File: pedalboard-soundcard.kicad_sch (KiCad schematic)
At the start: 5 parts, among them J1 RPi_GPIO

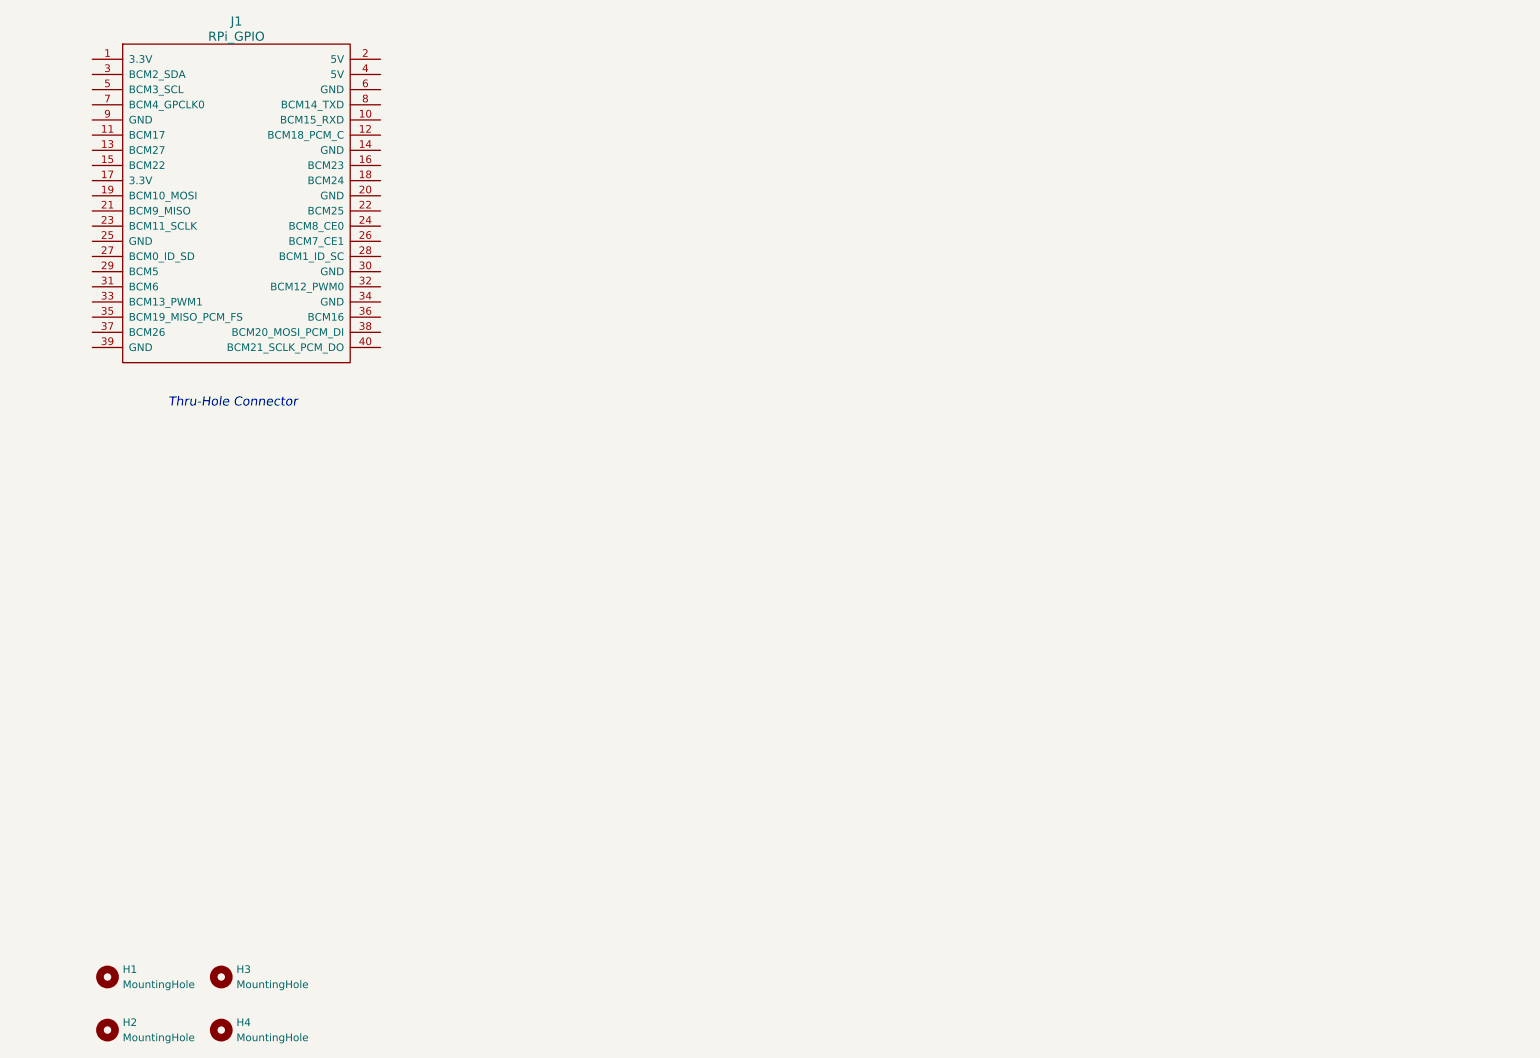
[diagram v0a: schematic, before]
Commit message: First placement of parts on PCB
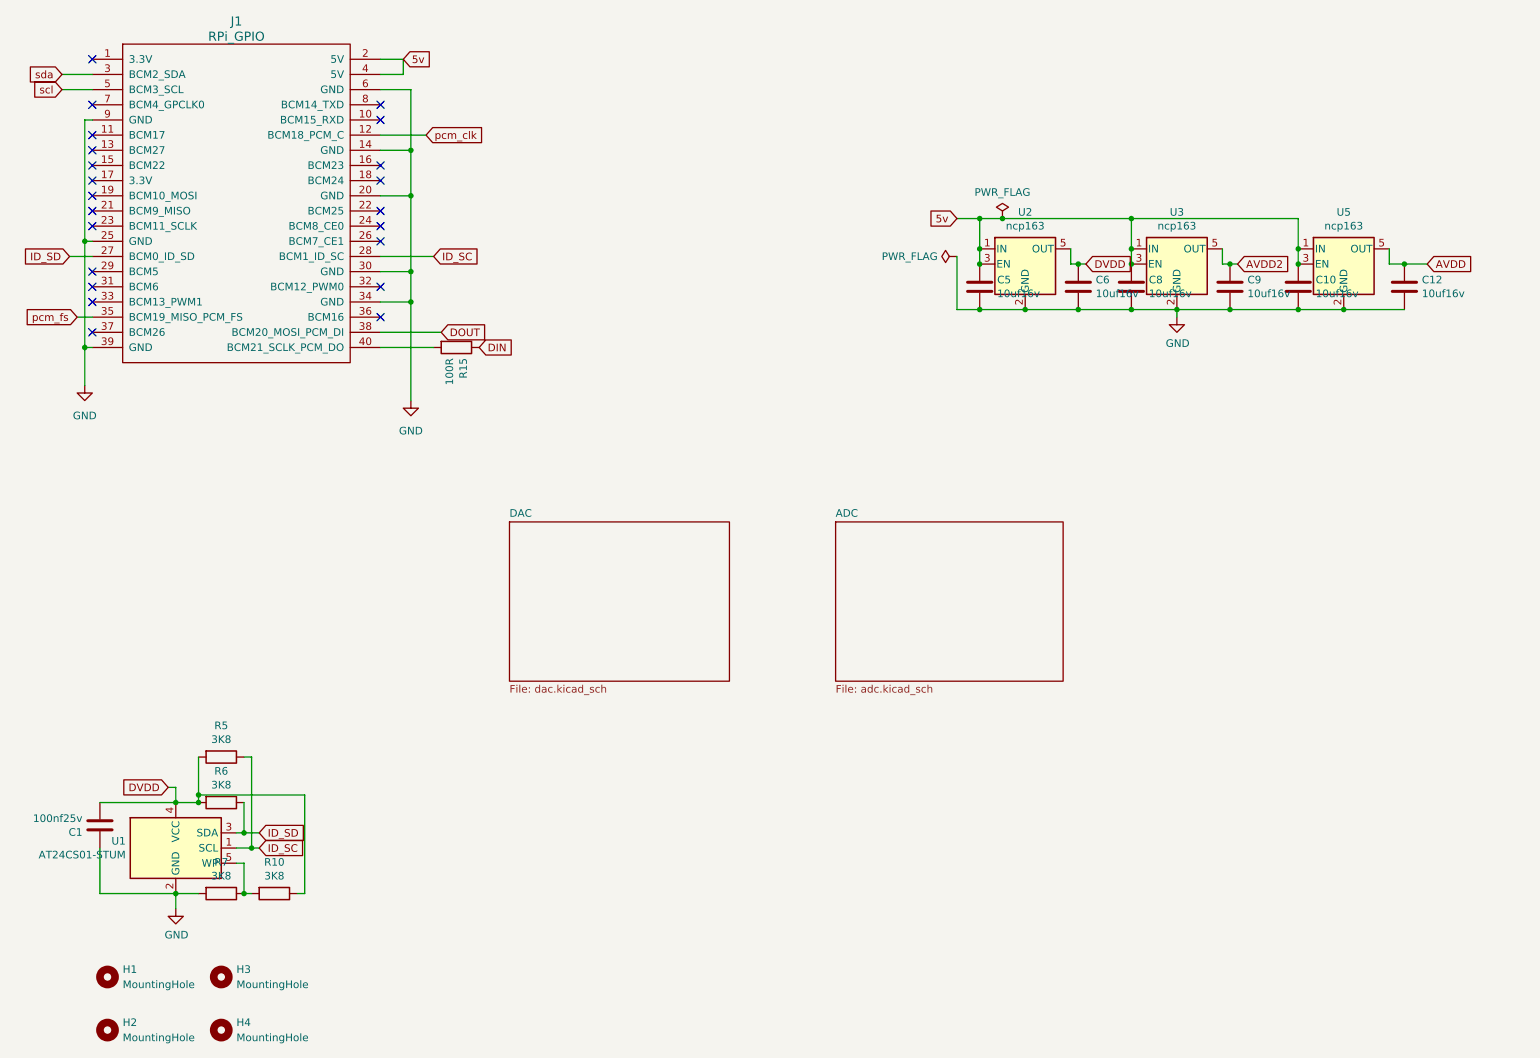
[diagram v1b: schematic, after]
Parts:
- added C1: 100nf25v, Capacitor_SMD:C_0805_2012Metric, symbol Device:C
- added C10, C12, C5, C6, C8, C9: 10uf16v, Capacitor_SMD:C_0805_2012Metric, symbol Device:C
- added R10, R5, R6, R7: 3K8, Resistor_SMD:R_0805_2012Metric, symbol Device:R
- added R15: 100R, Resistor_SMD:R_0805_2012Metric, symbol Device:R
- added U1: AT24CS01-STUM, Package_TO_SOT_SMD:SOT-23-5, symbol Memory_EEPROM:AT24CS01-STUM
- added U2, U3, U5: ncp163, Package_TO_SOT_SMD:SOT-23-5, symbol zynthiandac-rescue:TLV71333PDBV-Regulator_Linear
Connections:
- net pcm_clk: now reaches J1.12 (BCM18_PCM_C)
- net GND: now reaches J1.14 (GND)
- net GND: now also J1.20 (GND), J1.25 (GND), J1.30 (GND), J1.34 (GND), J1.39 (GND), J1.6 (GND), J1.9 (GND), C1.1, C10.2, C12.2, C5.2, C6.2, C8.2, C9.2, R7.2, U1.2 (GND), U2.2 (GND), U3.2 (GND), U5.2 (GND)
- net 5v: now reaches J1.2 (5V)
- net 5v: now also J1.4 (5V), C10.1, C5.1, C8.1, U2.1 (IN), U2.3 (EN), U3.1 (IN), U3.3 (EN), U5.1 (IN), U5.3 (EN)
- net ID_SD: now reaches J1.27 (BCM0_ID_SD)
- net ID_SD: now also R6.1, U1.3 (SDA)
- net ID_SC: now reaches J1.28 (BCM1_ID_SC)
- net ID_SC: now also R5.1, U1.1 (SCL)
- net sda: now reaches J1.3 (BCM2_SDA)
- net pcm_fs: now reaches J1.35 (BCM19_MISO_PCM_FS)
- net DOUT: now reaches J1.38 (BCM20_MOSI_PCM_DI)
- net at J1.40 (BCM21_SCLK_PCM_DO): now also R15.2
- net scl: now reaches J1.5 (BCM3_SCL)
- new net: R10.2, R7.1, U1.5 (WP)
- new net AVDD: C12.1, U5.5 (OUT)
- new net AVDD2: C9.1, U3.5 (OUT)
- new net DIN: R15.1
- new net DVDD: C1.2, C6.1, R10.1, R5.2, R6.2, U1.4 (VCC), U2.5 (OUT)
- no-connect marks 0 -> 22
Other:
- added sheet ADC (adc.kicad_sch)
- added sheet DAC (dac.kicad_sch)
- note removed: "Thru-Hole Connector"

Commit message: Page settings
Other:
- company: (none) -> github.com/pedalboard
- title: (none) -> Open Pedalboard Soundcard
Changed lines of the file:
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@@
 (kicad_sch (version 20230121) (generator eeschema)
   (paper "A4")
+  (title_block
+    (title "Open Pedalboard Soundcard")
+    (date "2023-12-19")
+    (rev "0.0.1")
+    (company "github.com/pedalboard")
+    (comment 1 "Source Code: https://github.com/pedalboard/pedalboard-hw")
+    (comment 2 "License: CERN Open Hardware Licence Version 2 - Permissive")
+  )
   (junction (at 172.72 68.58) (diameter 0) (color 0 0 0 0)
   )

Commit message: Distribute parts on PCB
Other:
- moved on the sheet: C1, R10, R5, R6, R7, U1

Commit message: Cleanup placement
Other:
- moved on the sheet: C10, C12, C5, C6, C8, C9, U2, U3, U5

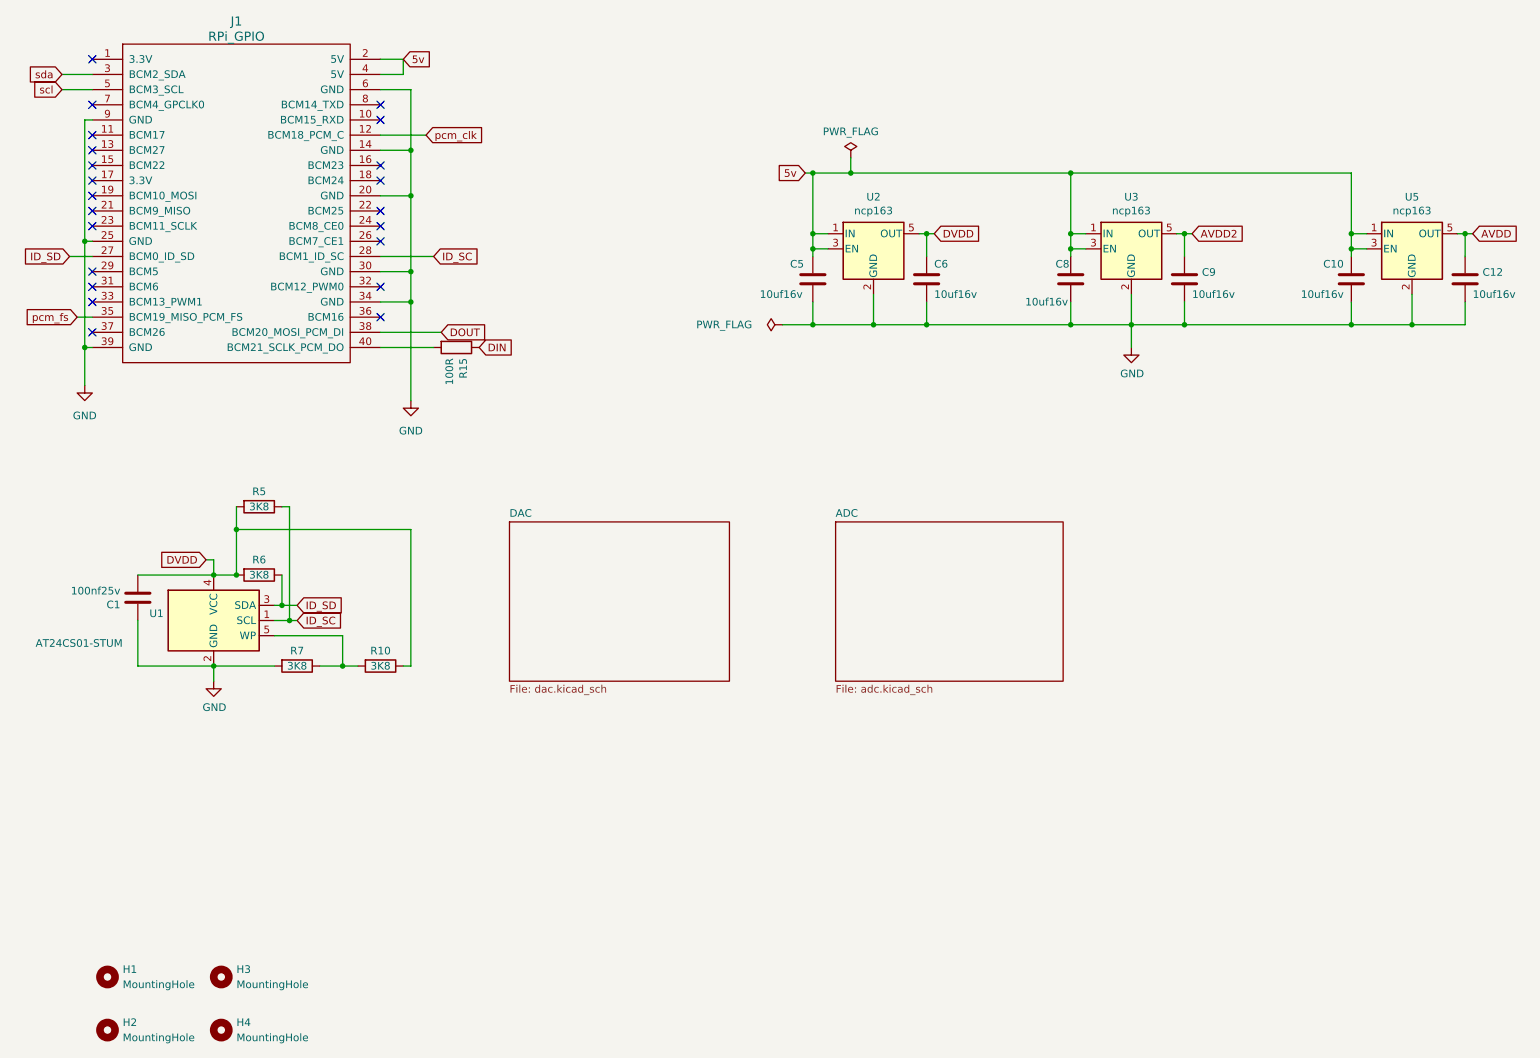
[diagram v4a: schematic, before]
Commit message: improve BOM
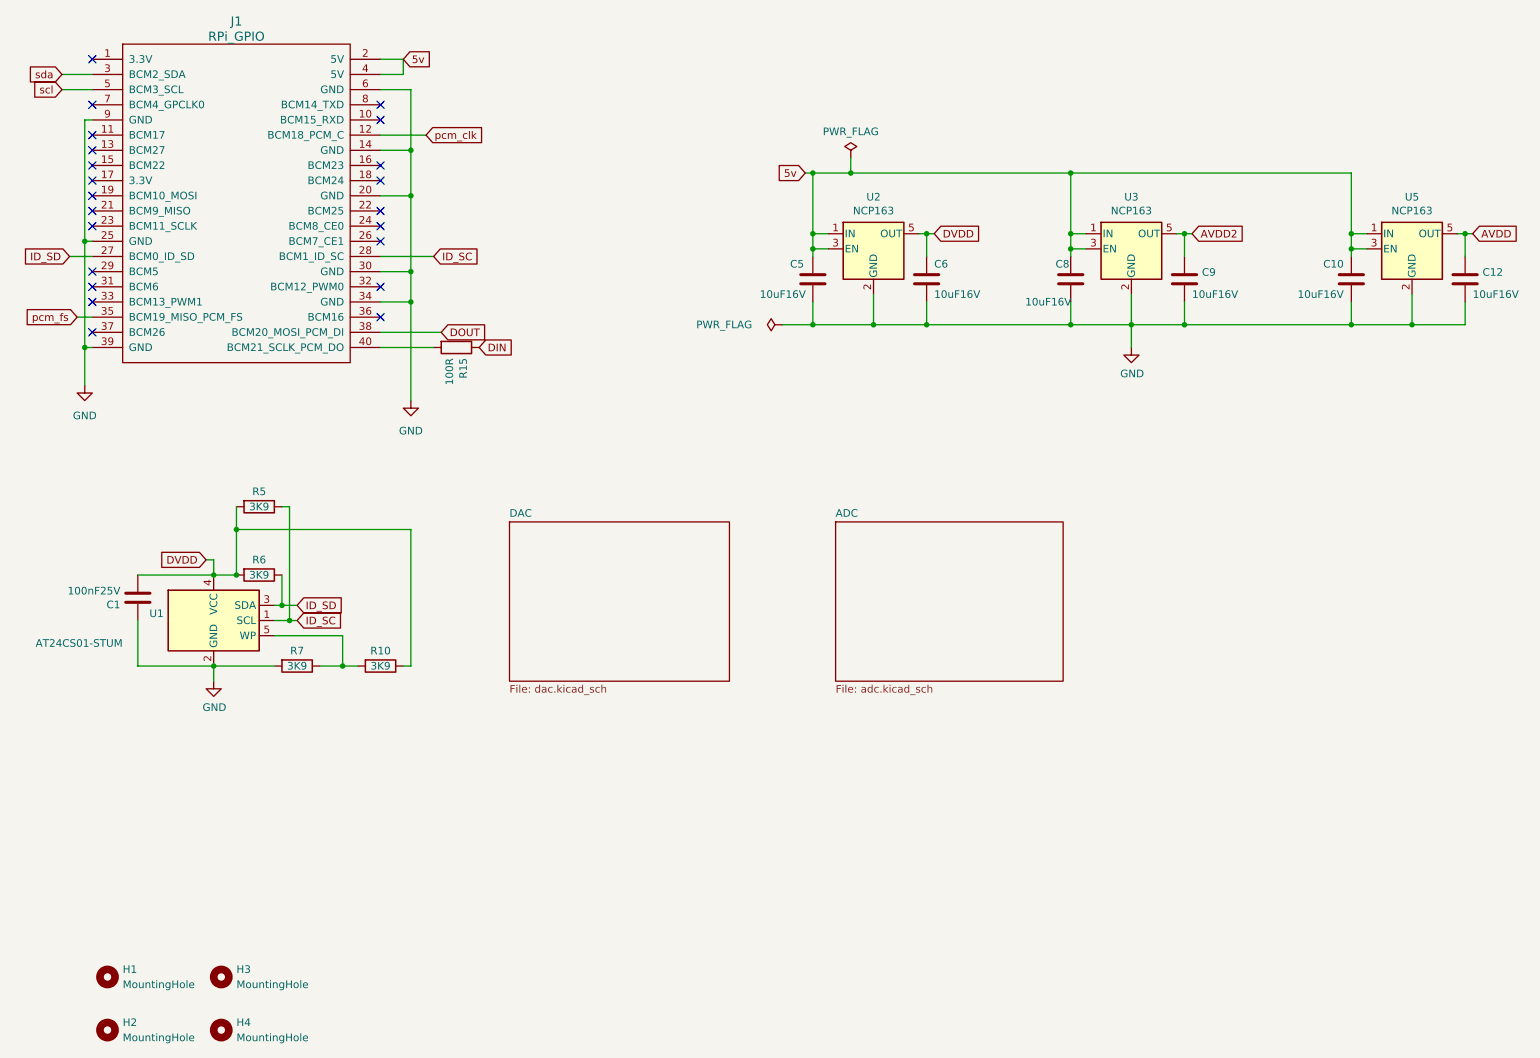
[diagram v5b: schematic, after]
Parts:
- C1: value 100nf25v -> 100nF25V; Supplier (none) -> https://www.digikey.ch/de/products/detail/samsung-electro-m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
- C10, C12, C5, C6, C8, C9: value 10uf16v -> 10uF16V; Supplier (none) -> https://www.digikey.ch/de/products/detail/samsung-electro-m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
- R10, R5, R6, R7: value 3K8 -> 3K9; Supplier (none) -> https://www.digikey.ch/de/products/detail/stackpole-electro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
- R15: Supplier (none) -> https://www.digikey.ch/de/products/detail/stackpole-electro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
- U1: Supplier (none) -> https://www.digikey.ch/de/products/detail/microchip-technol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
- U2, U3, U5: value ncp163 -> NCP163; Supplier (none) -> https://www.digikey.ch/de/products/detail/onsemi/NCP163ASN3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

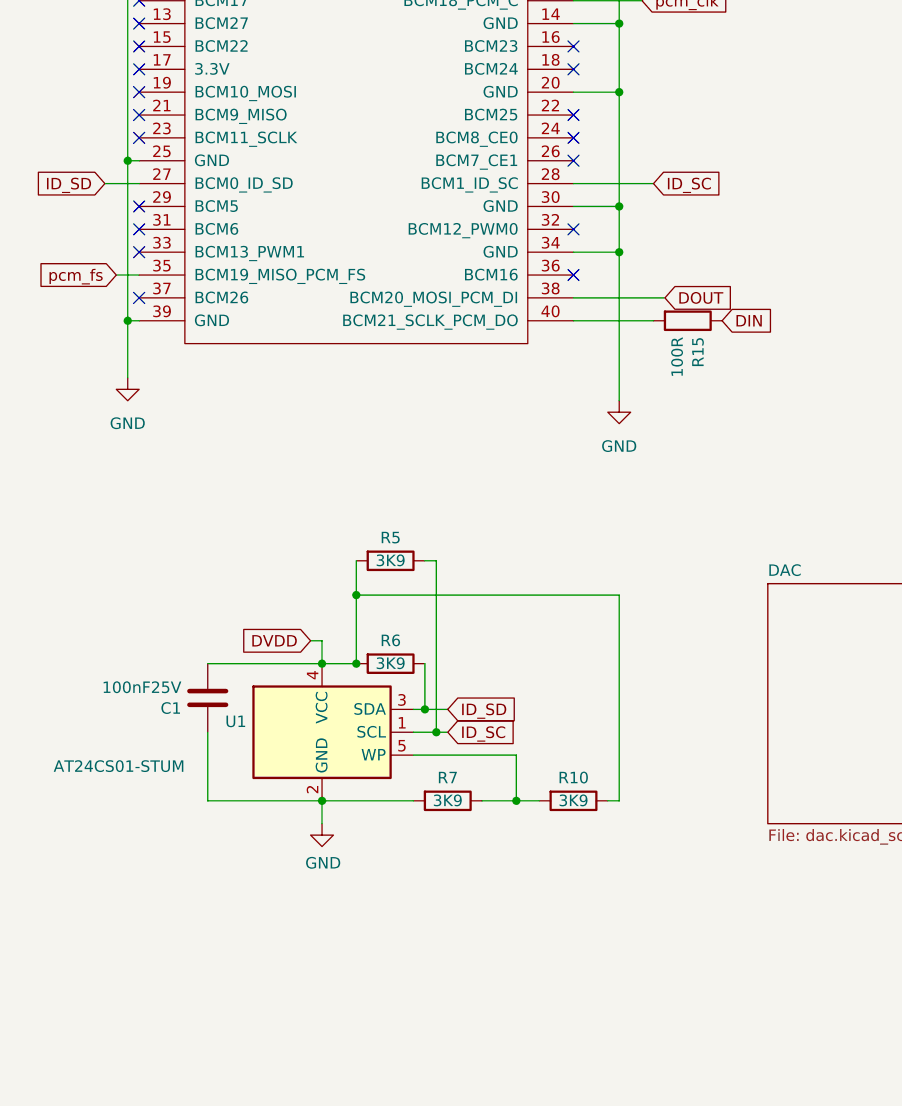
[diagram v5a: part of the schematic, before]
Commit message: Cleanup schematic for eeprom
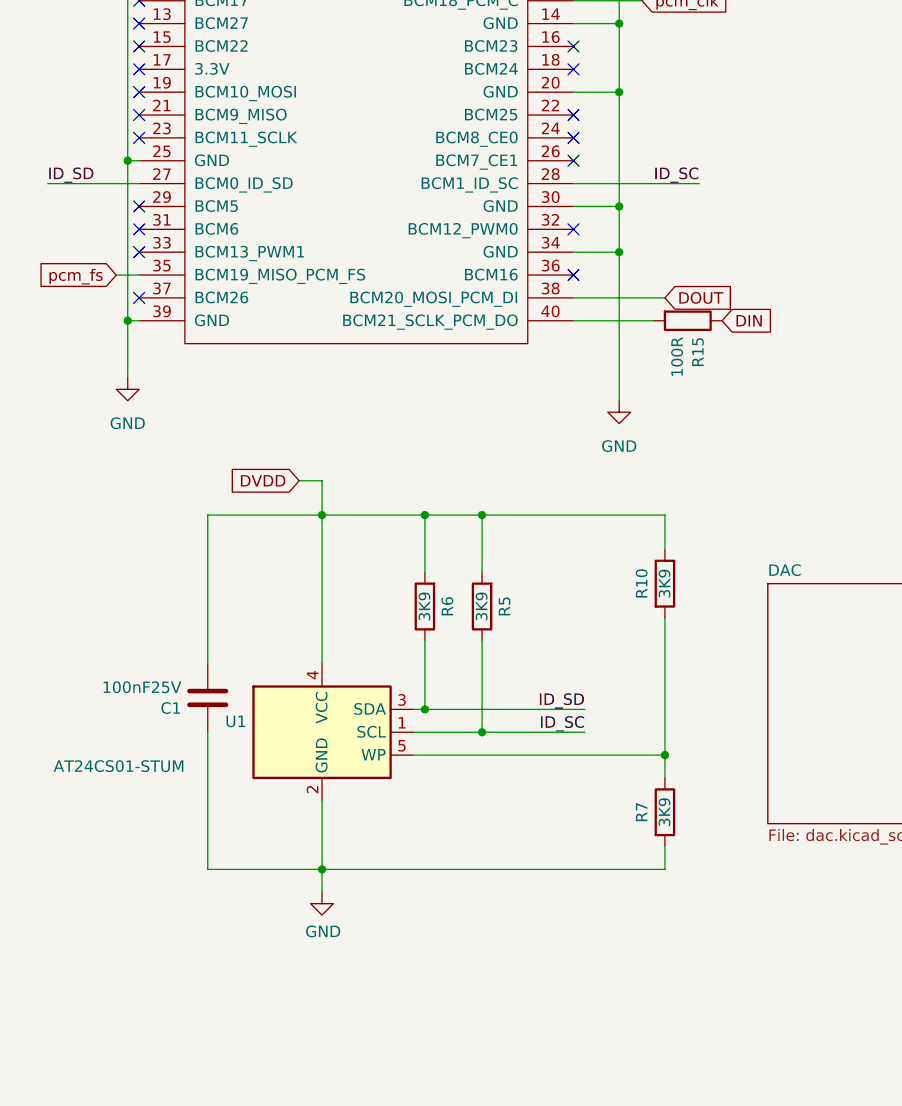
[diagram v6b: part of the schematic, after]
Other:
- moved on the sheet: R10, R5, R6, R7
